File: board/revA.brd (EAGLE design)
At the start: 40 x 50 mm, 28 parts, among them IC1 LM2931, U1 LDK120DM33R

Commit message: Updating values
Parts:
- added C4: 1uF 5v, rcl:C0603
- added R11: 10k, rcl:R0603
- D1, D2, D3, D4: value (none) -> 80V
- R10, R7, R8, R9: value (none) -> 470R
- moved D7 102.9 mm to (13.0, 24.0), turned to 180 degrees
- moved R6 98.4 mm to (3.00, 17.0), turned to 180 degrees
- moved D6 93.8 mm to (8.00, 24.0), turned to 180 degrees
- moved D5 84.7 mm to (3.00, 24.0), turned to 180 degrees
- moved R5 80.9 mm to (13.0, 17.0)
- moved R4 80.3 mm to (13.0, 20.0)
- moved R3 71.8 mm to (8.00, 17.0), turned to 180 degrees
- moved R2 71.2 mm to (8.00, 20.0), turned to 180 degrees
- moved R1 65.1 mm to (3.00, 20.0), turned to 180 degrees
- moved C2 46.3 mm to (7.00, 43.0), turned to 90 degrees
- moved C6 41.3 mm to (3.00, 30.0)
- moved C7 35.5 mm to (7.00, 34.0), turned to 90 degrees
- moved C5 32.8 mm to (3.00, 28.0)
- moved C3 27.7 mm to (7.00, 39.0), turned to 270 degrees
- moved C1 25.0 mm to (3.63, 46.7), turned to 90 degrees
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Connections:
- removed net VBAT: MCU.1
- removed net VDDA: MCU.9
- removed net VDD_1: MCU.24
- removed net VDD_2: MCU.36
- removed net VDD_3: MCU.48
- removed net VSSA: MCU.8
- removed net VSS_1: MCU.23
- removed net VSS_2: MCU.35
- removed net VSS_3: MCU.47
- new net N$1: C4.1, R11.2
- new net NRST: C4.2, MCU.7
- net +3V3: now also MCU.1, MCU.24, MCU.36, MCU.44, MCU.48, MCU.9, R11.1
- net GND: now also MCU.23, MCU.35, MCU.47, MCU.8

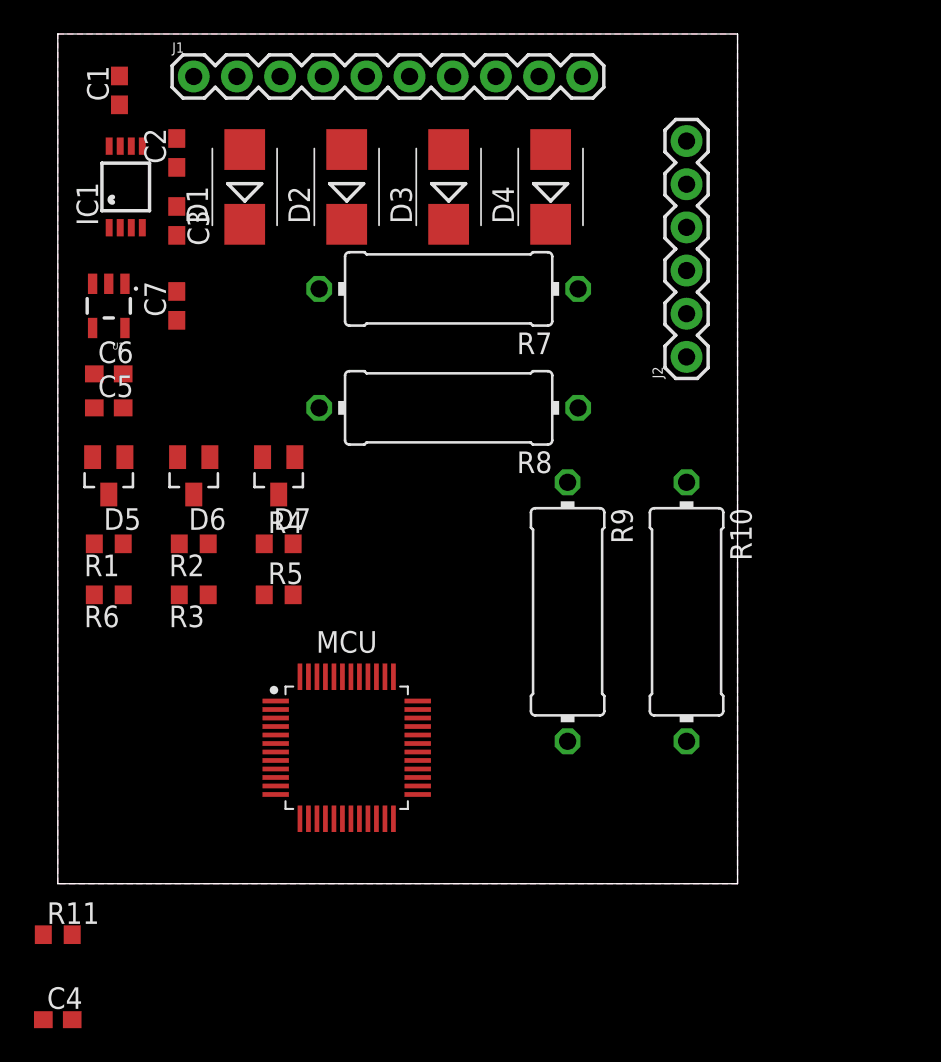
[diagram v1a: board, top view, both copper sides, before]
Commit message: Some routing, adding mosfets
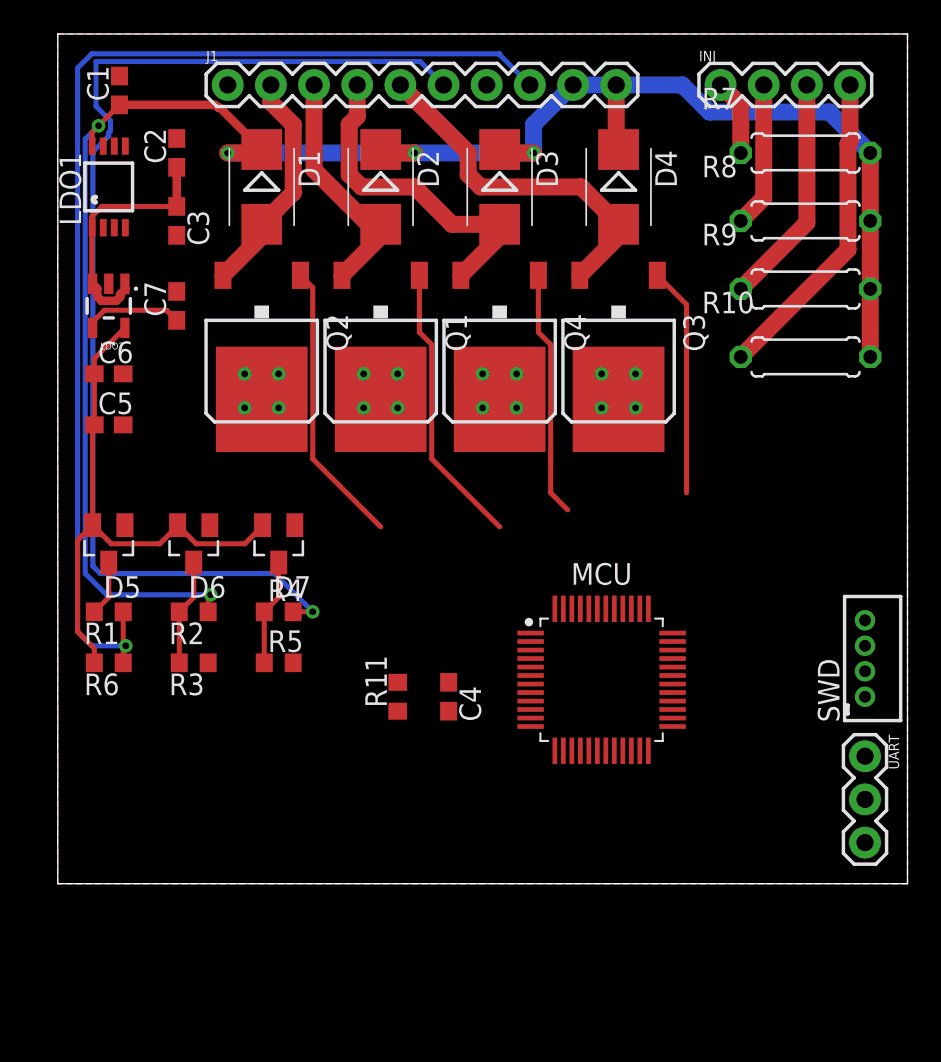
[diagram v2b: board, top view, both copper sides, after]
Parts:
- removed IC1: LM2931, national-semiconductor:MINI-SO8
- removed J2: (no value), SparkFun-Connectors:1X06
- added INJ: (no value), SparkFun-Connectors:1X04
- added LDO1: LM2931, national-semiconductor:MINI-SO8
- added Q1, Q2, Q3, Q4: VND7NV04, transistor-power:D-PAK_TO252AA
- added SWD: B4B-ZR, con-jst:B4B-ZR
- added UART: (no value), SparkFun-Connectors:1X03
- R10, R7, R8, R9: value 470R -> 1K; device rcl:0414/15 -> rcl:0207/7
- moved C4 29.8 mm to (23.0, 11.0), turned to 270 degrees
- moved R11 24.4 mm to (20.0, 11.0), turned to 90 degrees
- moved R8 23.7 mm to (44.0, 39.0), turned to 0 degrees
- moved R9 23.6 mm to (44.0, 35.0), turned to 0 degrees
- moved R7 22.5 mm to (44.0, 43.0), turned to 0 degrees
- moved R10 16.6 mm to (44.0, 31.0), turned to 0 degrees
- moved MCU 15.5 mm to (32.0, 12.0)
- moved D4 4.00 mm to (33.0, 41.0), turned to 270 degrees
- moved D5 4.00 mm to (3.00, 20.0)
- moved D6 4.00 mm to (8.00, 20.0)
- moved D7 4.00 mm to (13.0, 20.0)
- moved R1 4.00 mm to (3.00, 16.0)
- moved R2 4.00 mm to (8.00, 16.0)
- moved R3 4.00 mm to (8.00, 13.0)
- moved R4 4.00 mm to (13.0, 16.0)
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- renumbered U1 to LDO2
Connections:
- new net INJ1_TRIGGER: MCU.42, Q2.1
- new net INJ2_TRIGGER: MCU.43, Q1.1
- new net INJ3_TRIGGER: MCU.45, Q4.1
- new net INJ4_TRIGGER: MCU.46, Q3.1
- new net RXD: MCU.31, UART.2
- new net SWCLK: MCU.37, SWD.1
- new net SWDIO: MCU.34, SWD.3
- new net TXD: MCU.30, UART.3
- net +5V: now also LDO1.1; no longer IC1.1
- net GND: now also LDO1.7, Q1.4, Q2.4, Q3.4, Q4.4, SWD.2, UART.1; no longer IC1.7, J2.1
- net INJ1: now also Q2.3
- net INJ1_FAKE: now also INJ.1; no longer J2.5
- net INJ2: now also Q1.3
- net INJ2_FAKE: now also INJ.2; no longer J2.4
- net INJ3: now also Q4.3
- net INJ3_FAKE: now also INJ.3; no longer J2.3
- net INJ4: now also Q3.3
- net INJ4_FAKE: now also INJ.4; no longer J2.2
- net NRST: now also SWD.4
- net VCC: now also LDO1.8; no longer IC1.8, J2.6
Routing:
- net VCC: track 0.00 -> 112.4 mm, vias 0 -> 5
- net FF_SIG: track 0.00 -> 67.2 mm, vias 0 -> 1
- net AN1: track 0.00 -> 66.7 mm, vias 0 -> 1
- net +3V3: track 0.00 -> 33.1 mm
- net INJ4: track 0.00 -> 20.9 mm
- net INJ3: track 0.00 -> 19.5 mm
- net INJ4_FAKE: track 0.00 -> 18.7 mm
- net INJ1_TRIGGER: track 0.00 -> 16.8 mm
- net INJ2_TRIGGER: track 0.00 -> 16.8 mm
- net INJ3_TRIGGER: track 0.00 -> 14.8 mm
- net +5V: track 0.00 -> 14.6 mm
- net INJ2: track 0.00 -> 14.5 mm
- net INJ3_FAKE: track 0.00 -> 13.6 mm
- net INJ4_TRIGGER: track 0.00 -> 13.5 mm
- net INJ1: track 0.00 -> 13.5 mm
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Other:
- board size 40 x 50 mm -> 50 x 50 mm

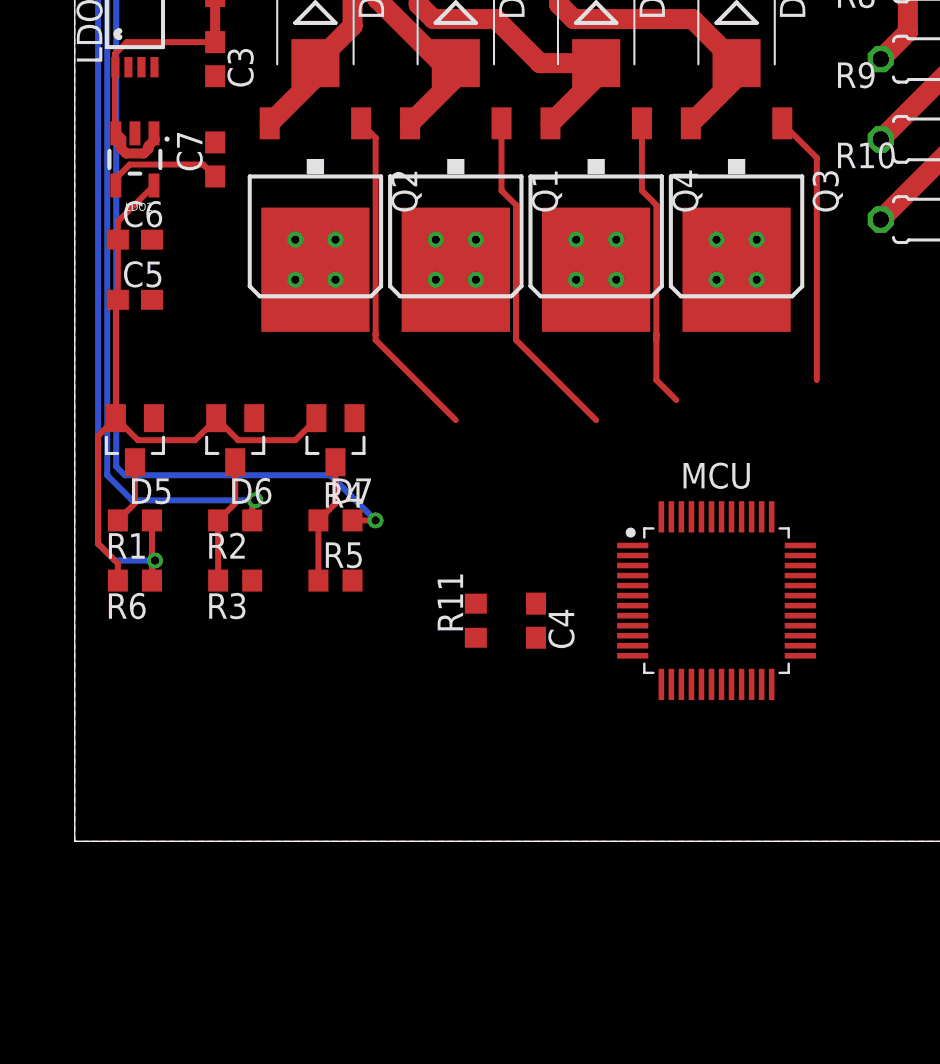
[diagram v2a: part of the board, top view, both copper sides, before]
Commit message: Adding buffer for mosfets
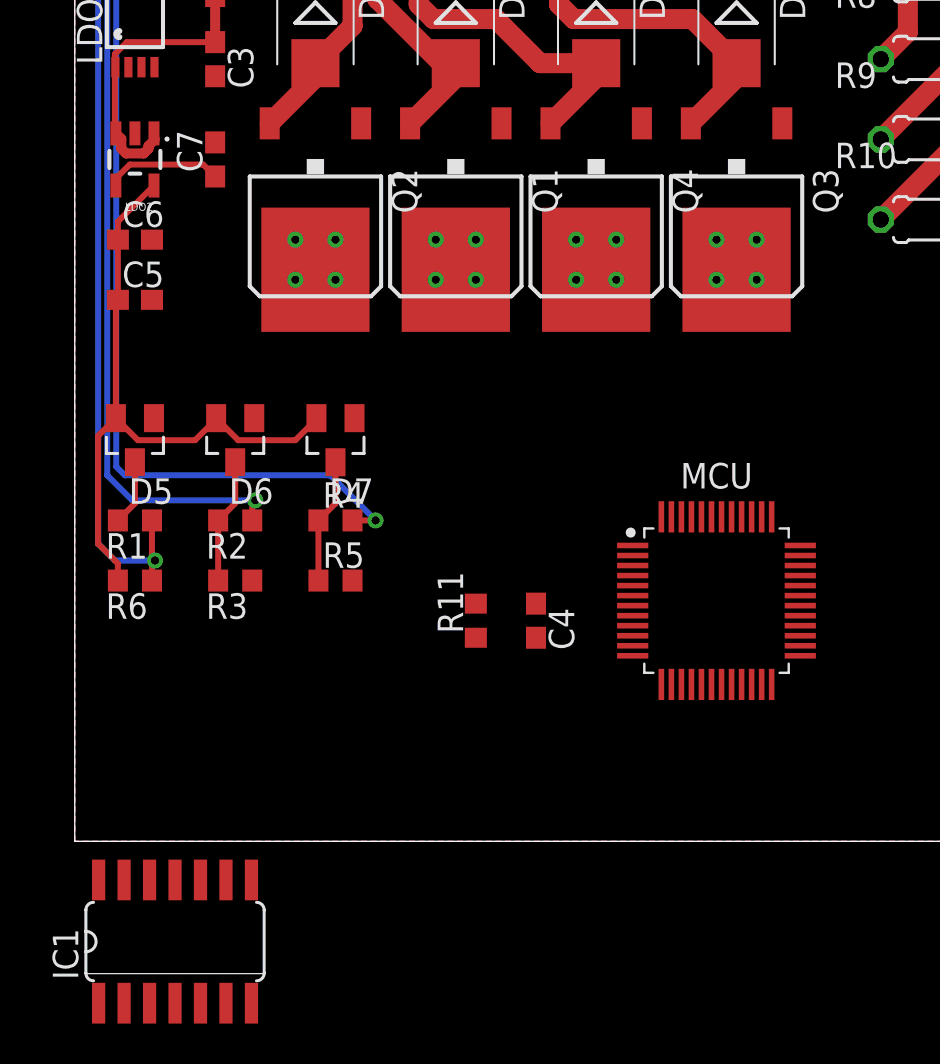
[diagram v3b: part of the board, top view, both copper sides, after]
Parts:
- added IC1: 74HCT125D, 74xx-eu:SO14
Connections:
- new net N$10: IC1.8, Q3.1
- new net N$7: IC1.6, Q2.1
- new net N$8: IC1.3, Q1.1
- new net N$9: IC1.11, Q4.1
- net +5V: now also IC1.14
- net GND: now also IC1.1, IC1.10, IC1.13, IC1.4, IC1.7
- net INJ1_TRIGGER: now also IC1.5; no longer Q2.1
- net INJ2_TRIGGER: now also IC1.2; no longer Q1.1
- net INJ3_TRIGGER: now also IC1.12; no longer Q4.1
- net INJ4_TRIGGER: now also IC1.9; no longer Q3.1
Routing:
- net INJ1_TRIGGER: track 16.8 -> 0.00 mm
- net INJ2_TRIGGER: track 16.8 -> 0.00 mm
- net INJ3_TRIGGER: track 14.8 -> 0.00 mm
- net INJ4_TRIGGER: track 13.5 -> 0.00 mm
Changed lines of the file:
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@@
 <attribute name="VALUE" x="45.468" y="8.77" size="0.6096" layer="27" font="vector" ratio="20" rot="R270"/>
+</element>
+<element name="IC1" library="74xx-eu" library_urn="urn:adsk.eagle:library:85" package="SO14" package3d_urn="urn:adsk.eagle:package:1010/2" value="74HCT125D" x="5" y="-5" smashed="yes">
+<attribute name="NAME" x="0.174" y="-6.905" size="1.27" layer="25" ratio="10" rot="R90"/>
+<attribute name="VALUE" x="1.825" y="-5.762" size="1.27" layer="27" ratio="10"/>
 </element>
 </elements>
@@
 <wire x1="2.55831875" y1="34.2977" x2="3.44168125" y2="34.2977" width="0.5" layer="1"/>
 <wire x1="3.44168125" y1="34.2977" x2="3.6774" y2="34.53341875" width="0.5" layer="1"/>
+<contactref element="IC1" pad="14"/>
 <wire x1="4" y1="35" x2="3.95" y2="35.3001" width="0" layer="19" extent="1-1"/>
+<wire x1="1.19" y1="-1.9266" x2="2.55831875" y2="34.2977" width="0" layer="19" extent="1-1"/>
 </signal>
 <signal name="+3V3">
@@
 <contactref element="SWD" pad="2"/>
 <contactref element="UART" pad="1"/>
+<contactref element="IC1" pad="7"/>
+<contactref element="IC1" pad="13"/>
+<contactref element="IC1" pad="10"/>
+<contactref element="IC1" pad="4"/>
+<contactref element="IC1" pad="1"/>
+<wire x1="5" y1="-8.0734" x2="1.19" y2="-8.0734" width="0" layer="19" extent="1-1"/>
+<wire x1="8.81" y1="-8.0734" x2="5" y2="-8.0734" width="0" layer="19" extent="1-1"/>
+<wire x1="6.27" y1="-1.9266" x2="5" y2="-8.0734" width="0" layer="19" extent="1-1"/>
+<wire x1="2.46" y1="-1.9266" x2="6.27" y2="-1.9266" width="0" layer="19" extent="1-1"/>
+<wire x1="8.85" y1="13" x2="6.27" y2="-1.9266" width="0" layer="19" extent="1-1"/>
 </signal>
 <signal name="VCC">
@@
 <signal name="INJ1_TRIGGER">
 <contactref element="MCU" pad="42"/>
-<contactref element="Q2" pad="1"/>
-<wire x1="15.0024" y1="25.27474375" x2="15" y2="25.27234375" width="0.3" layer="1"/>
-<wire x1="15" y1="25.27234375" x2="15" y2="25" width="0.3" layer="1"/>
-<wire x1="14.28" y1="35.8" x2="15.0024" y2="35.0776" width="0.3" layer="1"/>
-<wire x1="15.0024" y1="35.0776" x2="15.0024" y2="25.27474375" width="0.3" layer="1"/>
-<wire x1="15" y1="25" x2="19" y2="21" width="0.3" layer="1"/>
-<wire x1="19" y1="21" x2="32.25" y2="16.1783" width="0" layer="19" extent="1-1"/>
+<contactref element="IC1" pad="5"/>
+<wire x1="6.27" y1="-8.0734" x2="32.25" y2="16.1783" width="0" layer="19" extent="1-1"/>
 </signal>
 <signal name="INJ2_TRIGGER">
 <contactref element="MCU" pad="43"/>
-<contactref element="Q1" pad="1"/>
-<wire x1="21.28" y1="35.8" x2="21.28" y2="32.44765625" width="0.3" layer="1"/>
-<wire x1="22.0024" y1="24.9976" x2="26" y2="21" width="0.3" layer="1"/>
-<wire x1="21.28" y1="32.44765625" x2="22.0024" y2="31.72525625" width="0.3" layer="1"/>
-<wire x1="22.0024" y1="31.72525625" x2="22.0024" y2="24.9976" width="0.3" layer="1"/>
-<wire x1="26" y1="21" x2="31.75" y2="16.1783" width="0" layer="19" extent="1-1"/>
+<contactref element="IC1" pad="2"/>
+<wire x1="2.46" y1="-8.0734" x2="31.75" y2="16.1783" width="0" layer="19" extent="1-1"/>
 </signal>
 <signal name="INJ3_TRIGGER">
 <contactref element="MCU" pad="45"/>
-<contactref element="Q4" pad="1"/>
-<wire x1="29.0024" y1="31.72525625" x2="29.0024" y2="25.27474375" width="0.3" layer="1"/>
-<wire x1="28.28" y1="35.8" x2="28.28" y2="32.44765625" width="0.3" layer="1"/>
-<wire x1="29.0024" y1="25.27474375" x2="29" y2="25.27234375" width="0.3" layer="1"/>
-<wire x1="29" y1="25.27234375" x2="29" y2="25" width="0.3" layer="1"/>
-<wire x1="28.28" y1="32.44765625" x2="29.0024" y2="31.72525625" width="0.3" layer="1"/>
-<wire x1="29.0024" y1="25.27474375" x2="29.0024" y2="22.9976" width="0.3" layer="1"/>
-<wire x1="29.0024" y1="22.9976" x2="30" y2="22" width="0.3" layer="1"/>
-<wire x1="30.75" y1="16.1783" x2="30" y2="22" width="0" layer="19" extent="1-1"/>
+<contactref element="IC1" pad="12"/>
+<wire x1="3.73" y1="-1.9266" x2="30.75" y2="16.1783" width="0" layer="19" extent="1-1"/>
 </signal>
 <signal name="INJ4_TRIGGER">
 <contactref element="MCU" pad="46"/>
-<contactref element="Q3" pad="1"/>
-<wire x1="35.28" y1="35.8" x2="37" y2="34.08" width="0.3" layer="1"/>
-<wire x1="37" y1="34.08" x2="37" y2="23" width="0.3" layer="1"/>
-<wire x1="30.25" y1="16.1783" x2="37" y2="23" width="0" layer="19" extent="1-1"/>
+<contactref element="IC1" pad="9"/>
+<wire x1="7.54" y1="-1.9266" x2="30.25" y2="16.1783" width="0" layer="19" extent="1-1"/>
 </signal>
 <signal name="SWCLK">
@@
 <wire x1="36.1783" y1="12.25" x2="47.5" y2="4.96" width="0" layer="19" extent="1-1"/>
 </signal>
+<signal name="N$7">
+<contactref element="Q2" pad="1"/>
+<contactref element="IC1" pad="6"/>
+<wire x1="7.54" y1="-8.0734" x2="14.28" y2="35.8" width="0" layer="19" extent="1-1"/>
+</signal>
+<signal name="N$8">
+<contactref element="Q1" pad="1"/>
+<contactref element="IC1" pad="3"/>
+<wire x1="3.73" y1="-8.0734" x2="21.28" y2="35.8" width="0" layer="19" extent="1-1"/>
+</signal>
+<signal name="N$9">
+<contactref element="IC1" pad="11"/>
+<contactref element="Q4" pad="1"/>
+<wire x1="5" y1="-1.9266" x2="28.28" y2="35.8" width="0" layer="19" extent="1-1"/>
+</signal>
+<signal name="N$10">
+<contactref element="Q3" pad="1"/>
+<contactref element="IC1" pad="8"/>
+<wire x1="8.81" y1="-1.9266" x2="35.28" y2="35.8" width="0" layer="19" extent="1-1"/>
+</signal>
 </signals>
